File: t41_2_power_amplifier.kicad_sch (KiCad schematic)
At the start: 59 parts, among them J1 5-1814832-1, J2 5-1814832-1, J3 B2B-XH-A_LF__SN_, J4 INPUT, Q1 Q_NMOS_GSD, Q2 Q_NPN_BCE, Q3 Q_NMOS_GSD, Q4 Q_NPN_BCE, Q5 PMOS, Q6 Q_NPN_BCE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

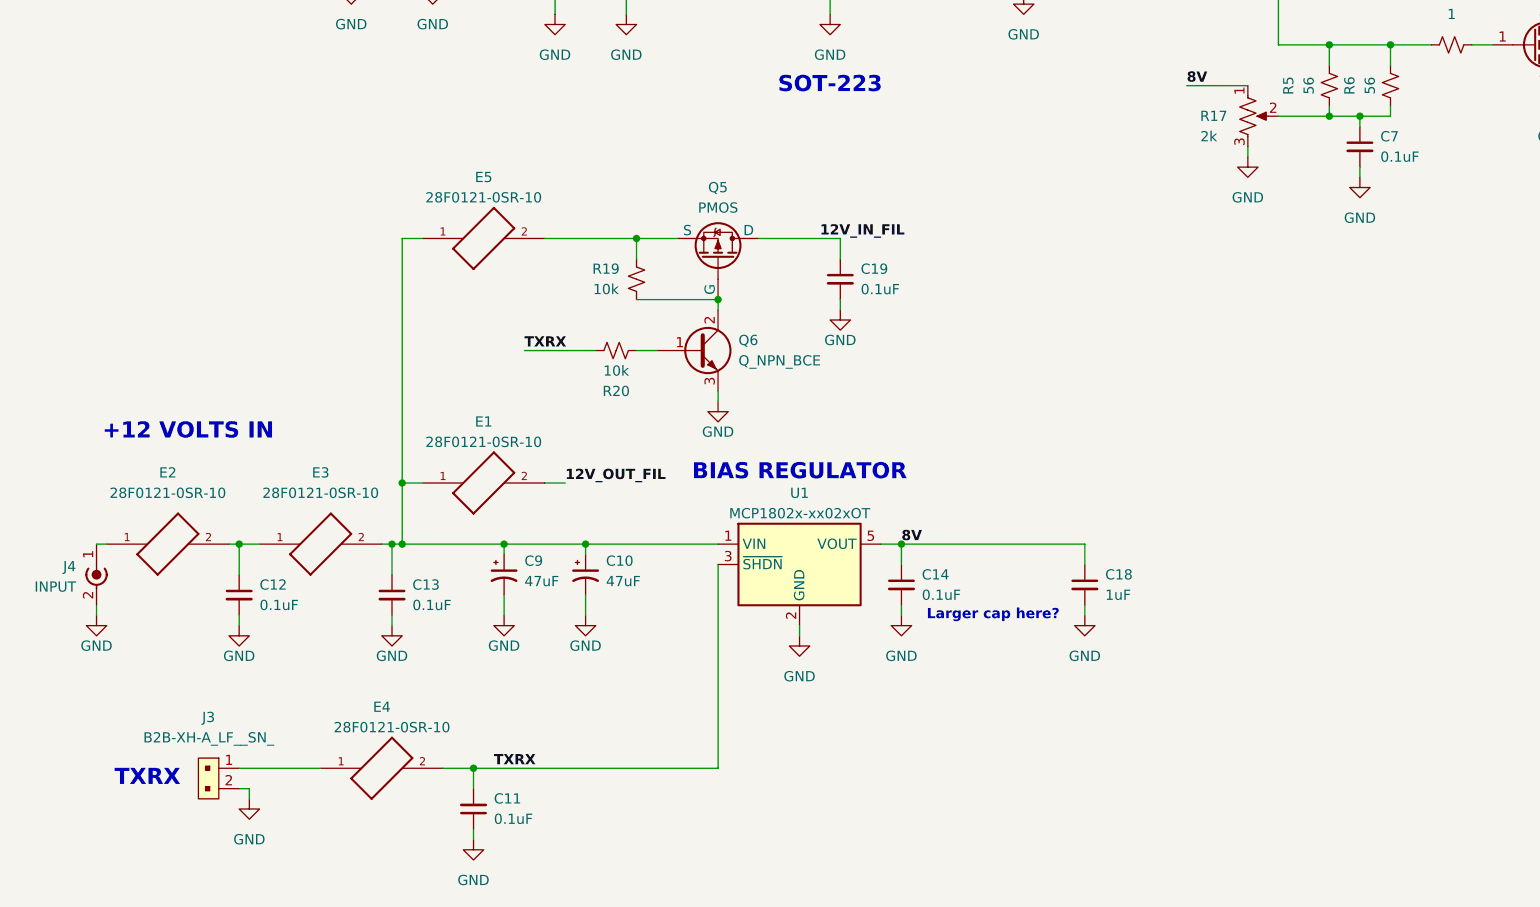
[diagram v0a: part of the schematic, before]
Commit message: Schematic complete, started on layout.
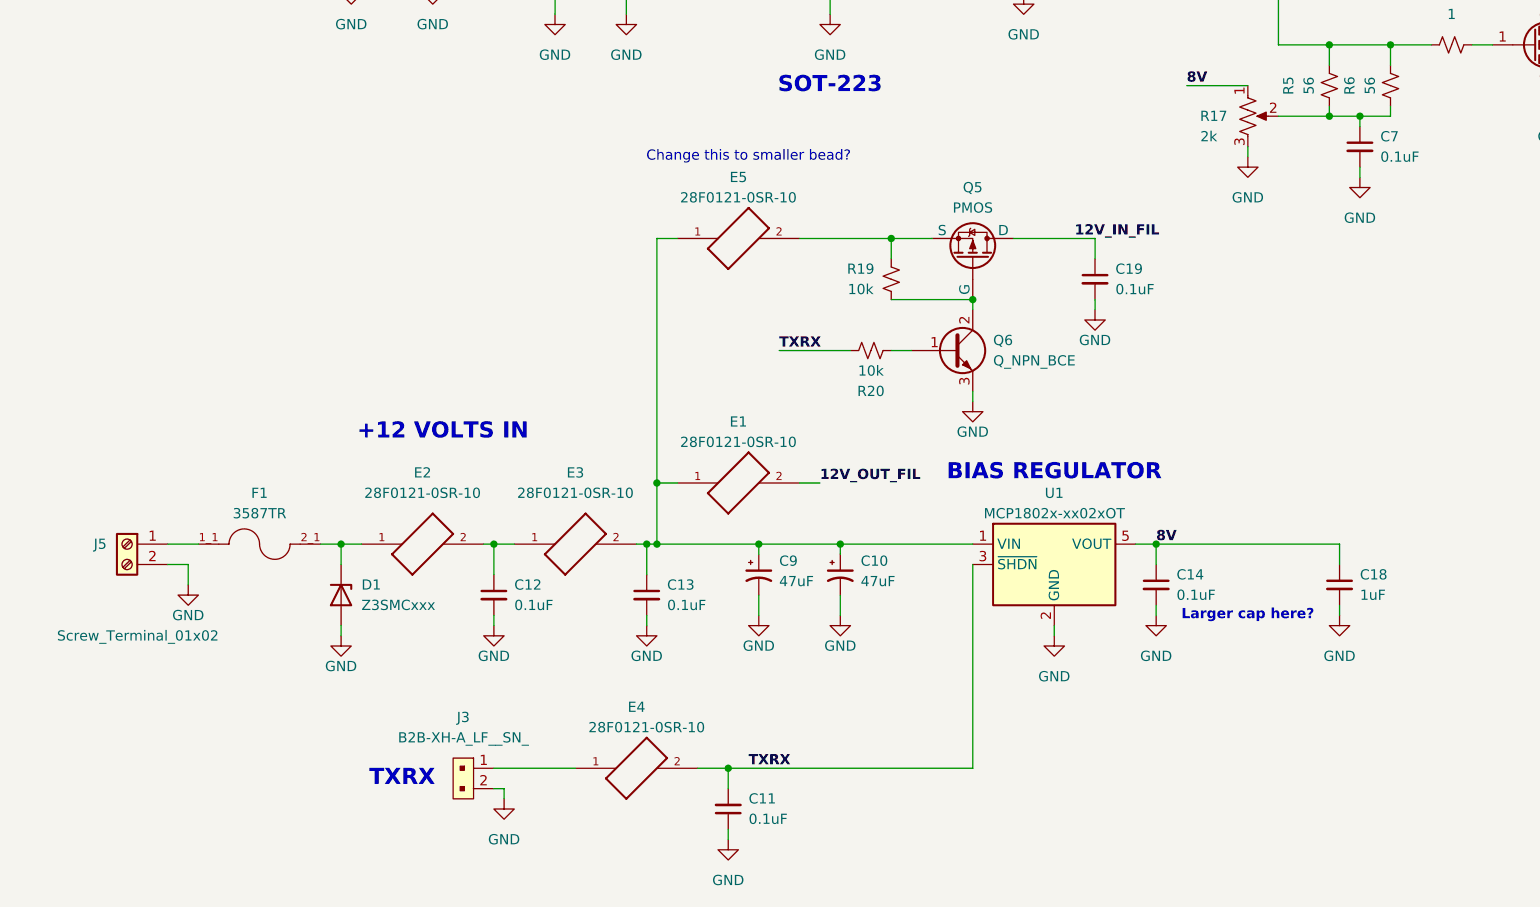
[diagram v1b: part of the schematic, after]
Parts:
- removed J4: INPUT, symbol Connector:Conn_Coaxial_Power
- added D1: Z3SMCxxx, Diode_SMD:D_SMC, symbol Diode:Z3SMCxxx
- added F1: 3587TR, 3587TR:FUSE_3587TR, symbol Auto_Fuse_Holder:3587TR
- added J5: Screw_Terminal_01x02, TerminalBlock_Philmore:TerminalBlock_Philmore_TB132_1x02_P5.00mm_Horizontal, symbol Connector:Screw_Terminal_01x02
- E1, E2, E3, E4, E5: footprint 28F0121-0SR-10:FB_28F0121-0SR-10 -> 28F0121_0SR_10:FB_28F0121-0SR-10
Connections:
- net GND: now also D1.2 (A), J5.2 (Pin_2)
- net at E2.1: now also D1.1 (K), F1.2_1
- new net: F1.1_1, J5.1 (Pin_1)
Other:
- note added: "Change this to smaller bead?"
- moved on the sheet: C10, C11, C12, C13, C14, C18, C19, C9, E1, E2, E3, E4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

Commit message: Finishing PCB placement.  Stopping point.
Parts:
- removed C4: 0.1uF, Capacitor_SMD:C_1206_3216Metric, symbol Device:C_Small
- removed R3, R4: DNP, Resistor_SMD:R_1206_3216Metric, symbol Device:R_Small_US
- removed T1: Transformer_1P_SS, Binocular_Core:BN-43-202_VERTICAL, symbol Device:Transformer_1P_SS
- added L2: ~, Binocular_Core:BN-43-202_VERTICAL, symbol InductorTapped:InductorTapped
- C2: value 180pF -> 100pF
- C3: value 0.1uF -> 100pF
- R14: value 56 -> 1000
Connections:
- net 12V_OUT_FIL: now also L2.2
- net at C2.2, Q1.3 (D), T2.2 (AB): now also C3.2, L2.3
- net at C16.2, L1.2, Q2.2 (C)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: now also Q4.4 (C); no longer Q4.2 (C)
- net at C2.1, Q3.3 (D), T2.1 (AA): now also C3.1, L2.1
- net at Q2.3 (E), R12.2: now also Q4.2 (B); no longer Q4.1 (B)
- net at Q4.3 (E), R13.2: now also Q4.1
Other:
- note added: "BFQ19 SOT-89"
- note added: "BFU590G SOT-223"
- note removed: "SOT-223"
- moved on the sheet: J1, R11, T2

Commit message: Routed.  Needs cleanup.
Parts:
- removed C19: 0.1uF, Capacitor_SMD:C_1206_3216Metric, symbol Device:C_Small
- removed Q5: PMOS, Package_TO_SOT_SMD:SOT-23, symbol Simulation_SPICE:PMOS
- removed Q6: Q_NPN_BCE, Package_TO_SOT_SMD:SOT-23, symbol Device:Q_NPN_BCE
- added C20: 1uf, Capacitor_SMD:C_1206_3216Metric, symbol Device:C_Small
- added C4: 0.1uF, Capacitor_SMD:C_1206_3216Metric, symbol Device:C_Small
- added Q5: Q_PMOS_GSD, Package_TO_SOT_SMD:SOT-23-3, symbol Device:Q_PMOS_GSD
- added Q6: Q_NPN_BEC, Package_TO_SOT_SMD:SOT-23-3, symbol Device:Q_NPN_BEC
- E4, E5: value 28F0121-0SR-10 -> XXX; footprint 28F0121_0SR_10:FB_28F0121-0SR-10 -> Inductor_SMD:L_1206_3216Metric
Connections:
- net 12V_IN_FIL: now also Q5.3 (D)
- net 12V_OUT_FIL: now also C4.1
- net GND: now also C20.2, C4.2, Q6.2 (E)
- net at C10.1, C13.1, C9.1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: now also C20.1
- net at R20.1: now also Q6.1 (B)
- net at R19.1: now also Q5.1 (G), Q6.3 (C)
- net at C8.2, R7.2, R8.2: now also R11.2
- net at E5.2, R19.2: now also Q5.2 (S)
- net at C5.1, R1.1, R7.1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: no longer R11.2
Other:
- note added: "P CHANNEL"
- note removed: "Change this to smaller bead?"
- moved on the sheet: C10, C9, E1

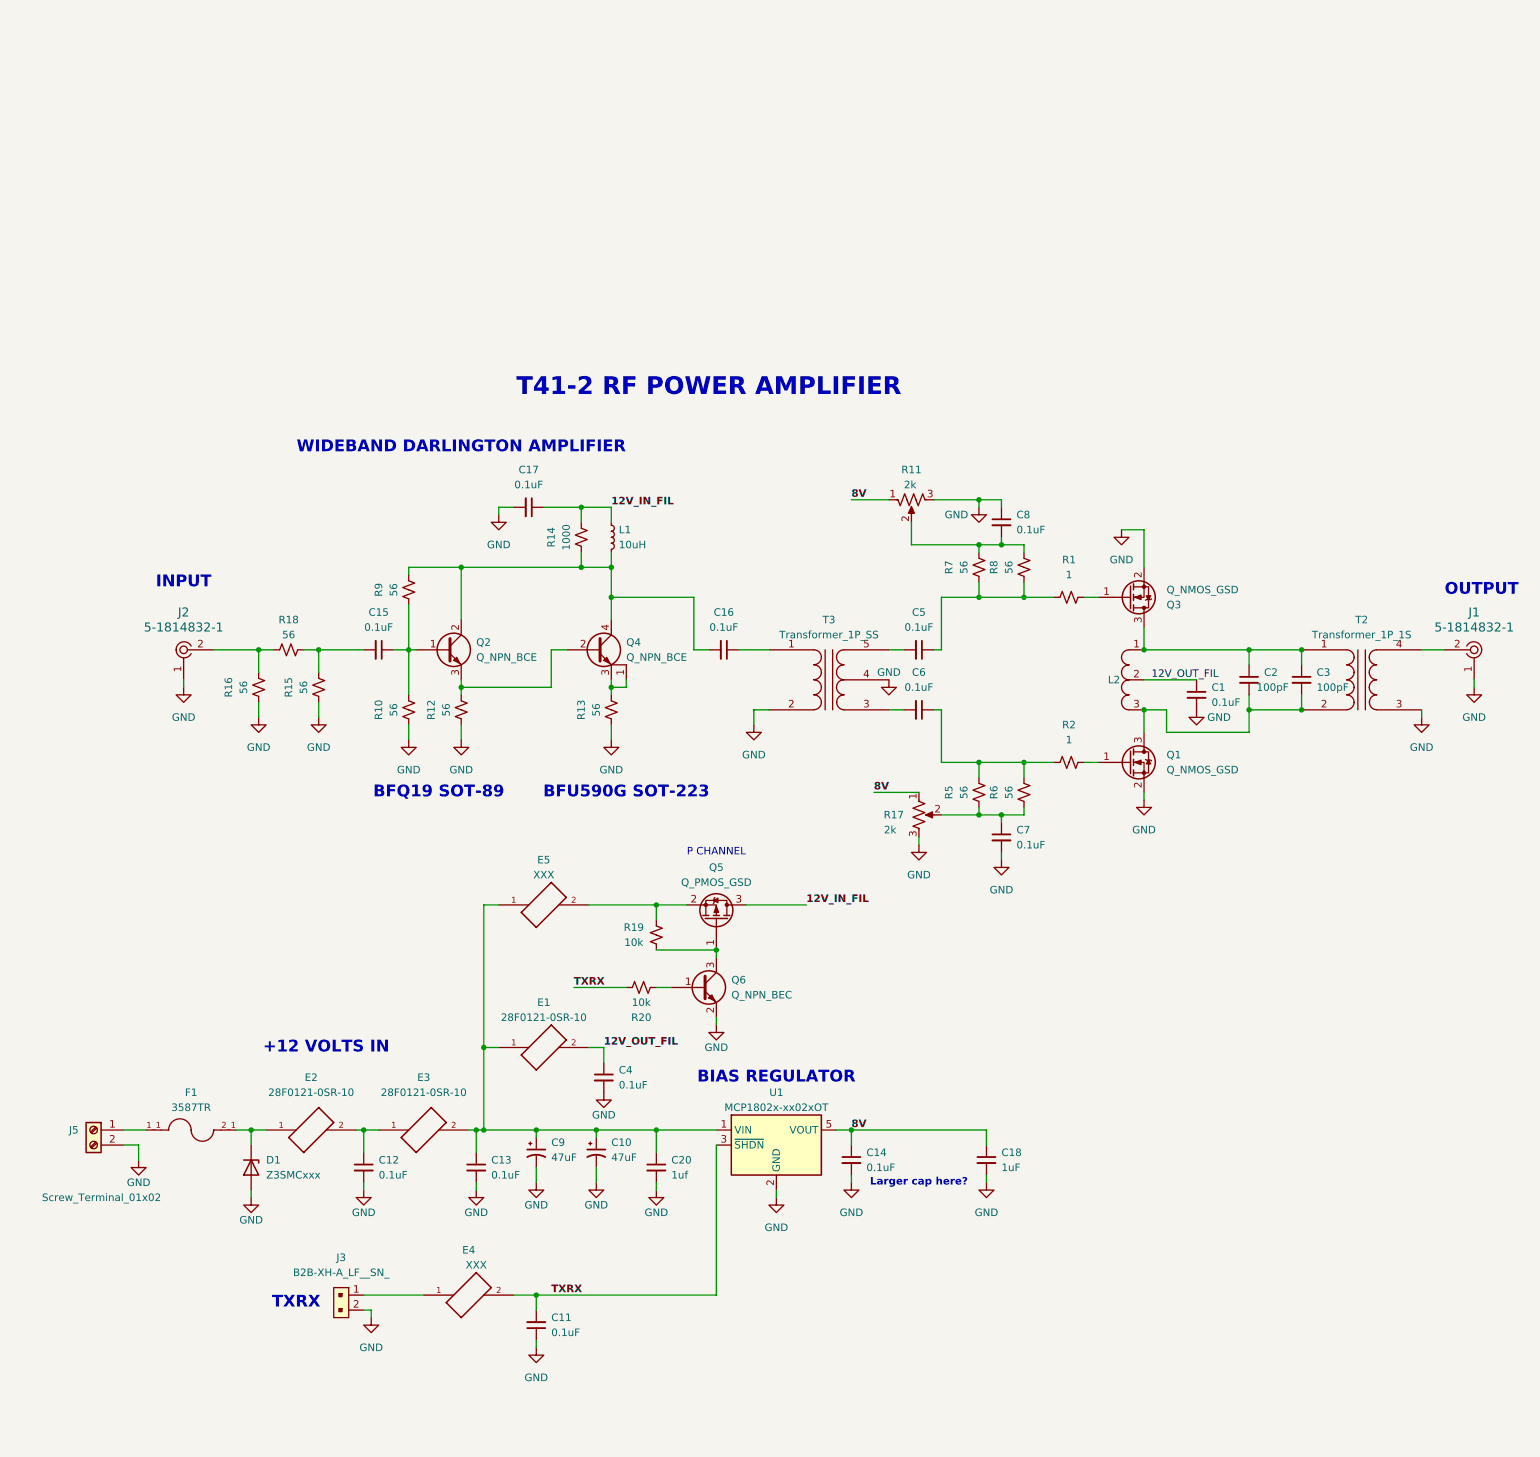
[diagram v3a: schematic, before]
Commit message: Added another stage to the input.
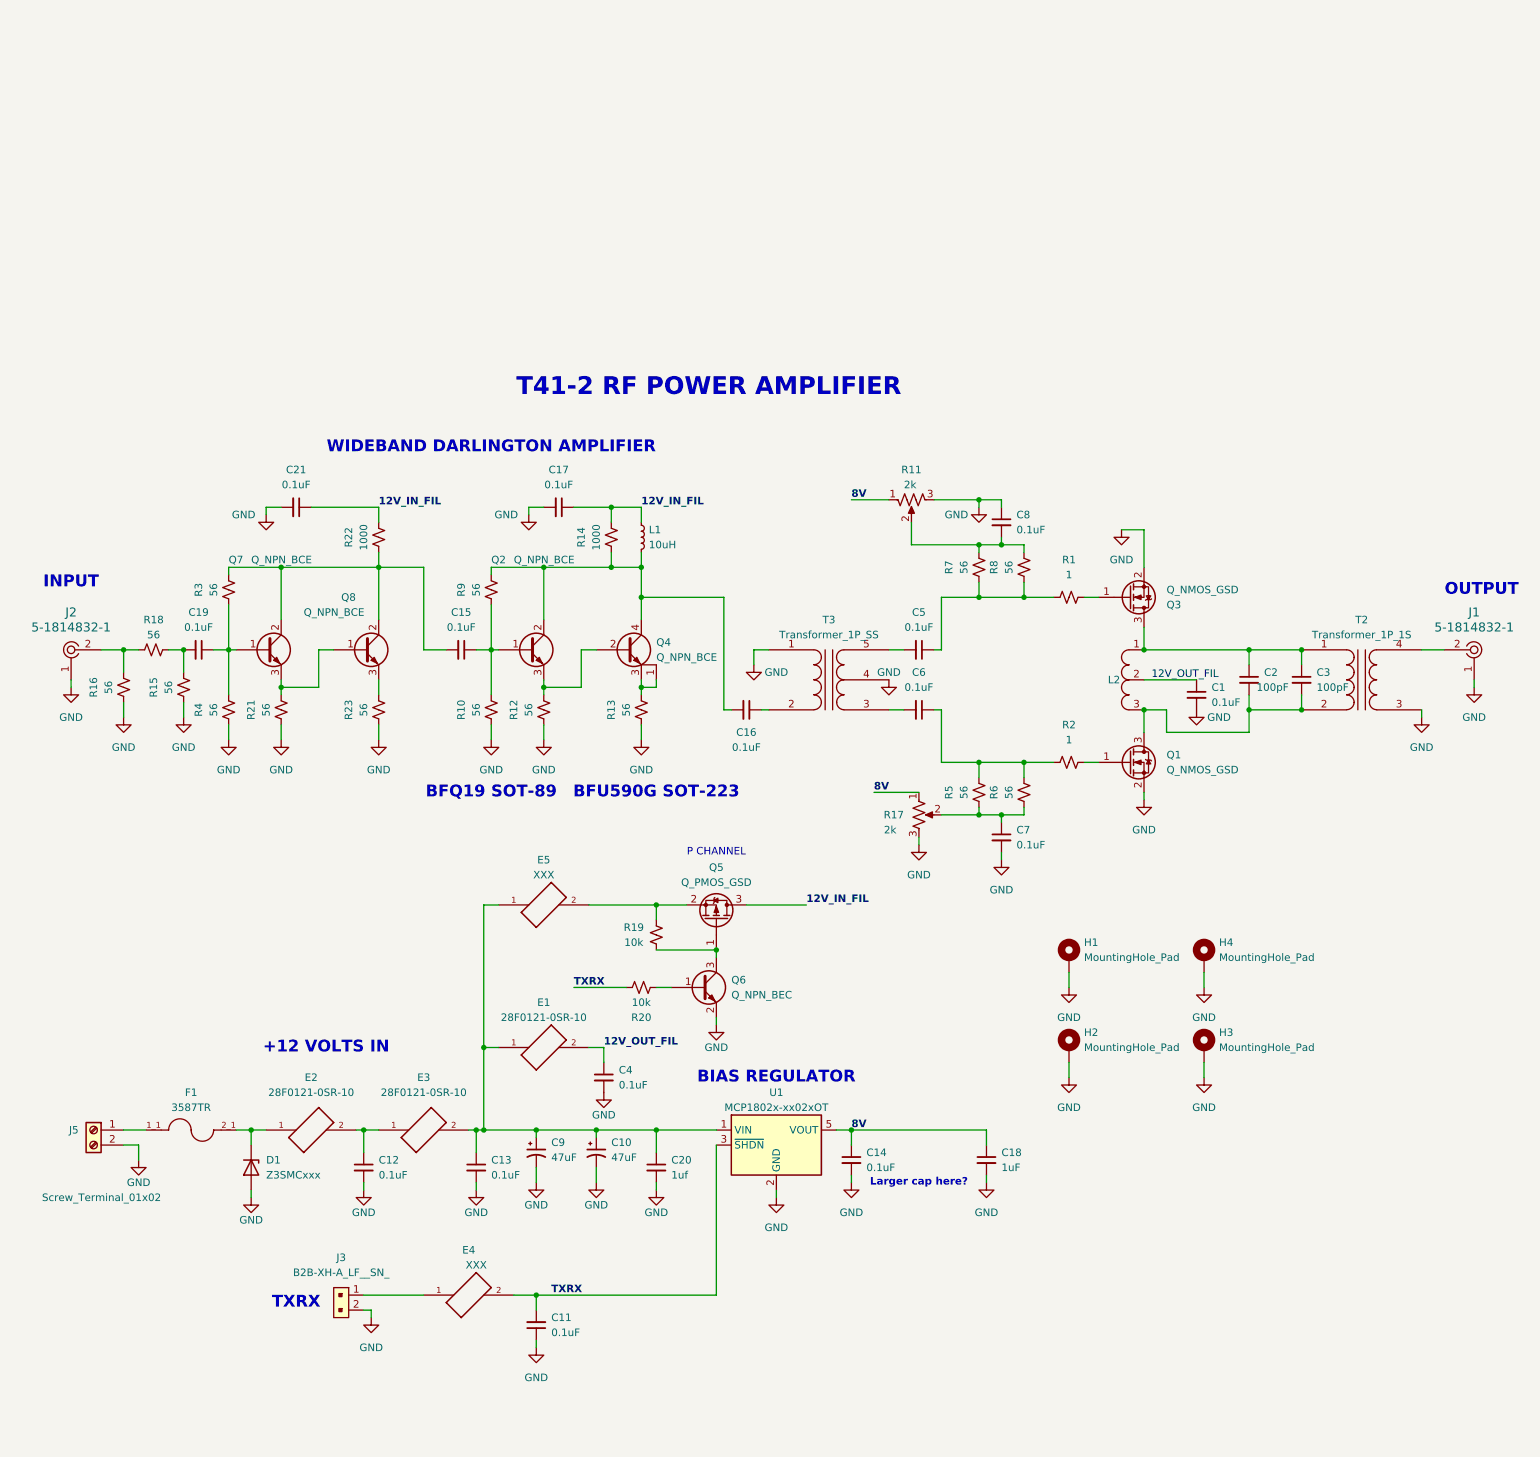
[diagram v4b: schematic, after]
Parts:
- added C19, C21: 0.1uF, Capacitor_SMD:C_1206_3216Metric, symbol Device:C_Small
- added H1, H2, H3, H4: MountingHole_Pad, MountingHole:MountingHole_4.3mm_M4_DIN965_Pad, symbol Mechanical:MountingHole_Pad
- added Q7, Q8: Q_NPN_BCE, Package_TO_SOT_SMD:SOT-23-3, symbol Device:Q_NPN_BCE
- added R21, R23, R3, R4: 56, Resistor_SMD:R_1206_3216Metric, symbol Device:R_Small_US
- added R22: 1000, Resistor_SMD:R_1206_3216Metric, symbol Device:R_Small_US
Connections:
- net 12V_IN_FIL: now also C21.1, R22.2
- net GND: now also T3.1 (AA), C21.2, H1.1, H2.1, H3.1, H4.1, R21.1, R23.1, R4.1; no longer T3.2 (AB)
- net at C16.1: now also T3.2 (AB); no longer T3.1 (AA)
- net at R15.2, R18.2: now also C19.2; no longer C15.2
- new net: Q8.3 (E), R23.2
- new net: Q7.3 (E), Q8.1 (B), R21.2
- new net: C15.2, Q7.2 (C), Q8.2 (C), R22.1, R3.2
- new net: C19.1, Q7.1 (B), R3.1, R4.2
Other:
- moved on the sheet: C15, C16, C17, J2, L1, Q2, Q4, R10, R12, R13, R14, R15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
